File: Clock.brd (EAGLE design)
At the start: 75.9 x 19 mm, 52 parts, among them IC1 A1301UA, U2 3.3V, U3 ATMEGA328

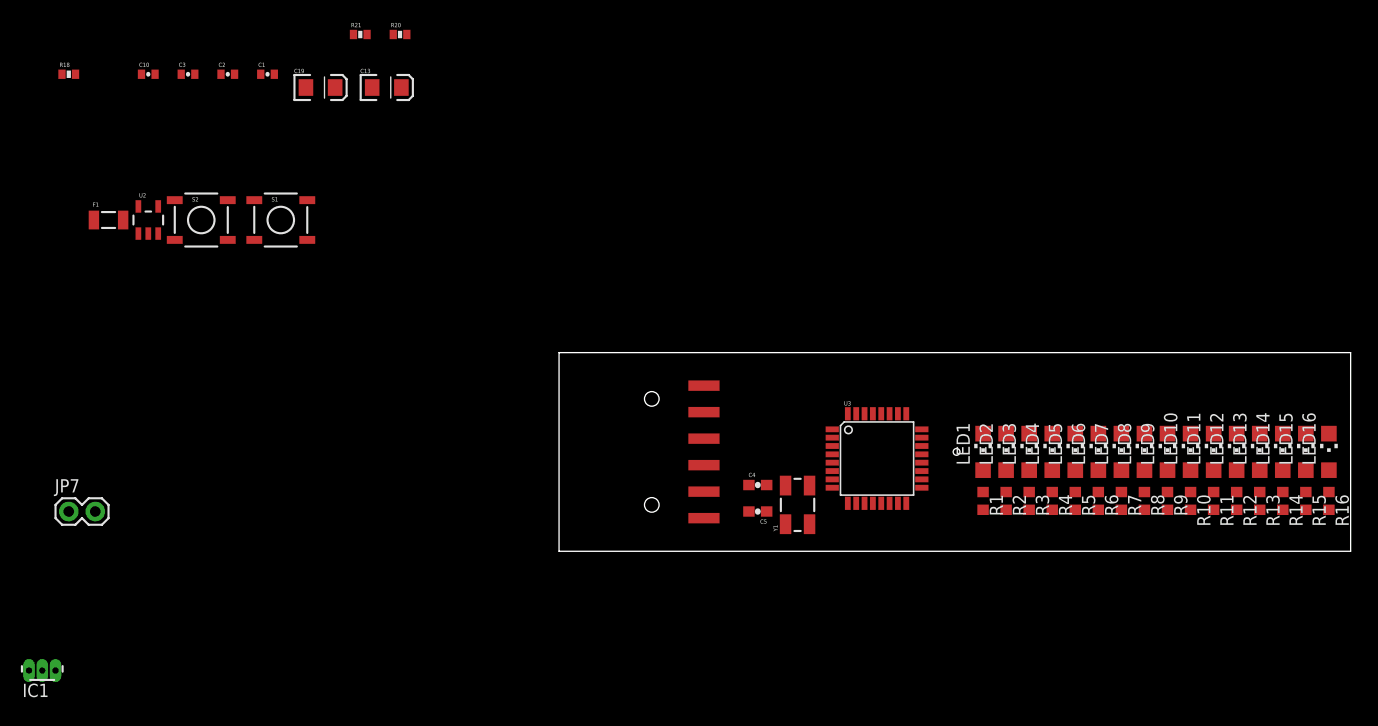
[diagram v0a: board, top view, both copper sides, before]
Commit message: Fully routed board
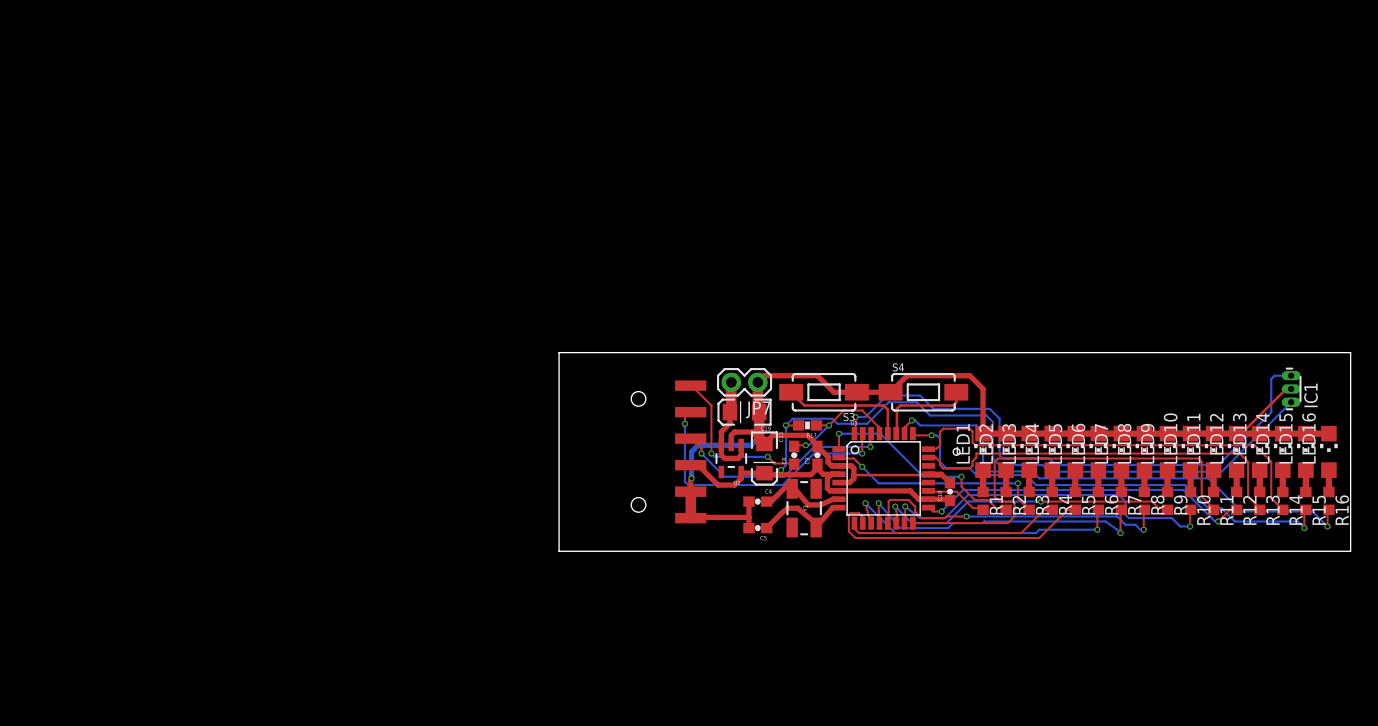
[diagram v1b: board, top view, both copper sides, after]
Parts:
- removed C1, C2, C3: 0.1uF, SparkFun:0402-CAP
- removed F1: 500mA-PTC, SparkFun:PTC-1206
- removed R18: 10K, SparkFun:0402-RES
- removed R20, R21: 1K, SparkFun:0402-RES
- removed S1, S2: Reset, SparkFun:TACTILE_SWITCH_SMD
- added C8, C9: 0.1uF, SparkFun-Passives:0603-CAP
- added R17: 10k, SparkFun-Passives:0603-RES
- added S3, S4: SWITCH-MOMENTARY-2SMD-1101NE, SparkFun-Electromechanical:TACTILE-SWITCH-1101NE
- C10: device SparkFun:0402-CAP -> SparkFun-Passives:0603-CAP
- moved IC1 122.7 mm to (70.2, 15.6), turned to 90 degrees
- moved C10 86.6 mm to (37.5, 5.71), turned to 90 degrees
- moved JP7 67.2 mm to (19.1, 16.2), turned to 180 degrees
- moved U2 60.4 mm to (16.5, 8.89), turned to 180 degrees
- moved C19 51.2 mm to (17.8, 13.3), turned to 180 degrees
- moved C13 50.7 mm to (19.7, 8.89), turned to 270 degrees
- moved U3 2.01 mm to (31.1, 6.99)
- moved C5 1.59 mm to (19.1, 2.22)
- moved C4 1.59 mm to (19.1, 4.76)
- moved JP9 1.27 mm to (7.62, 9.53)
- moved Y1 0.71 mm to (23.5, 4.13)
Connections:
- removed net AREF: C1.2, U3.20
- removed net N$25: F1.1
- removed net RX-IP: R20.1
- removed net TX-OP: R21.1
- new net A6: R1.2, U3.19
- net A4: now also S4.2; no longer S1.3, S1.4
- net A5: now also S3.2; no longer S2.3, S2.4
- net D2: now also IC1.3; no longer R1.2
- net DTR: now also C8.1; no longer C2.1
- net GND: now also C9.2, S3.1, S4.1; no longer C1.1, C3.1, S1.1, S1.2, S2.1, S2.2
- net RESET: now also C8.2, R17.1; no longer C2.2, R18.1
- net RX-I: no longer R21.2
- net TX-O: no longer R20.2
- net VCC: now also C9.1, R17.2; no longer C3.2, R18.2
- net VIN: now also JP7.2; no longer F1.2
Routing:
- net GND: track 0.00 -> 128.5 mm, vias 0 -> 1
- net VCC: track 0.00 -> 95.2 mm, vias 0 -> 2
- net D2: track 0.00 -> 54.4 mm, vias 0 -> 1
- net A3: track 0.00 -> 49.3 mm, vias 0 -> 2
- net A2: track 0.00 -> 44.7 mm, vias 0 -> 2
- net D12: track 0.00 -> 41.9 mm
- net A1: track 0.00 -> 41.4 mm
- net A0: track 0.00 -> 37.9 mm
- net D11: track 0.00 -> 33.9 mm, vias 0 -> 2
- net D13: track 0.00 -> 32.2 mm, vias 0 -> 2
- net D9: track 0.00 -> 30.2 mm, vias 0 -> 2
- net D10: track 0.00 -> 29.6 mm, vias 0 -> 2
- net D8: track 0.00 -> 29.2 mm, vias 0 -> 2
- net D7: track 0.00 -> 27.5 mm, vias 0 -> 2
- net TX-O: track 0.00 -> 27.3 mm, vias 0 -> 2
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
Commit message: Board updates for final board fab.
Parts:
- JP7: value External -> Vin
- turned IC1 to 270 degrees
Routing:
- net VCC: track 95.2 -> 100.9 mm
- net D2: track 54.4 -> 51.5 mm
- net GND: track 128.5 -> 130.2 mm
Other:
- board text added: "+"
- board text added: "POVClock Rev1 Paul and Shan Studios"
